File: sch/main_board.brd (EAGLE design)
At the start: 70 x 50 mm, 19 parts, among them IC1 MCP73831T-2ACI_OT, J1 MICRO_USB_B_HIROSE_ZX62-B-5PA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

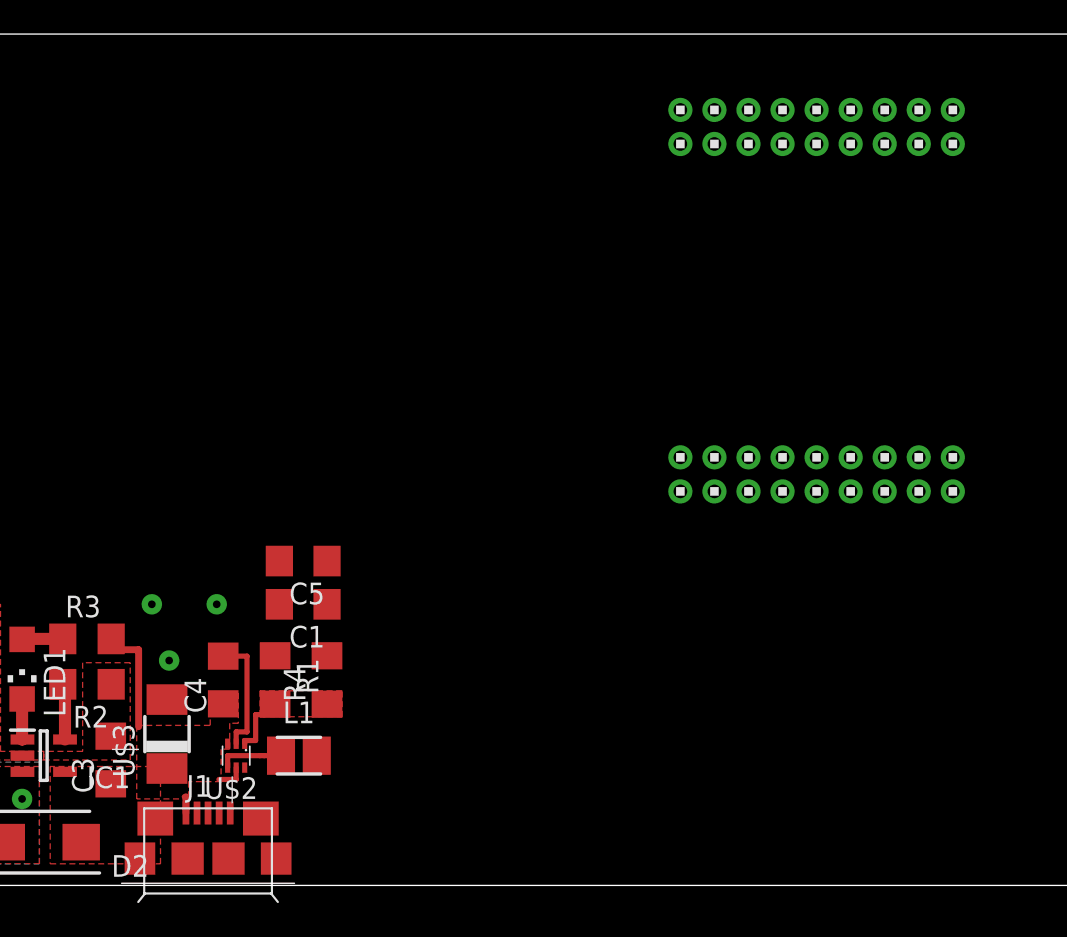
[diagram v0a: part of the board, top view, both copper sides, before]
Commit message: Add docs for STM32WB, Remove unused power supply elements.
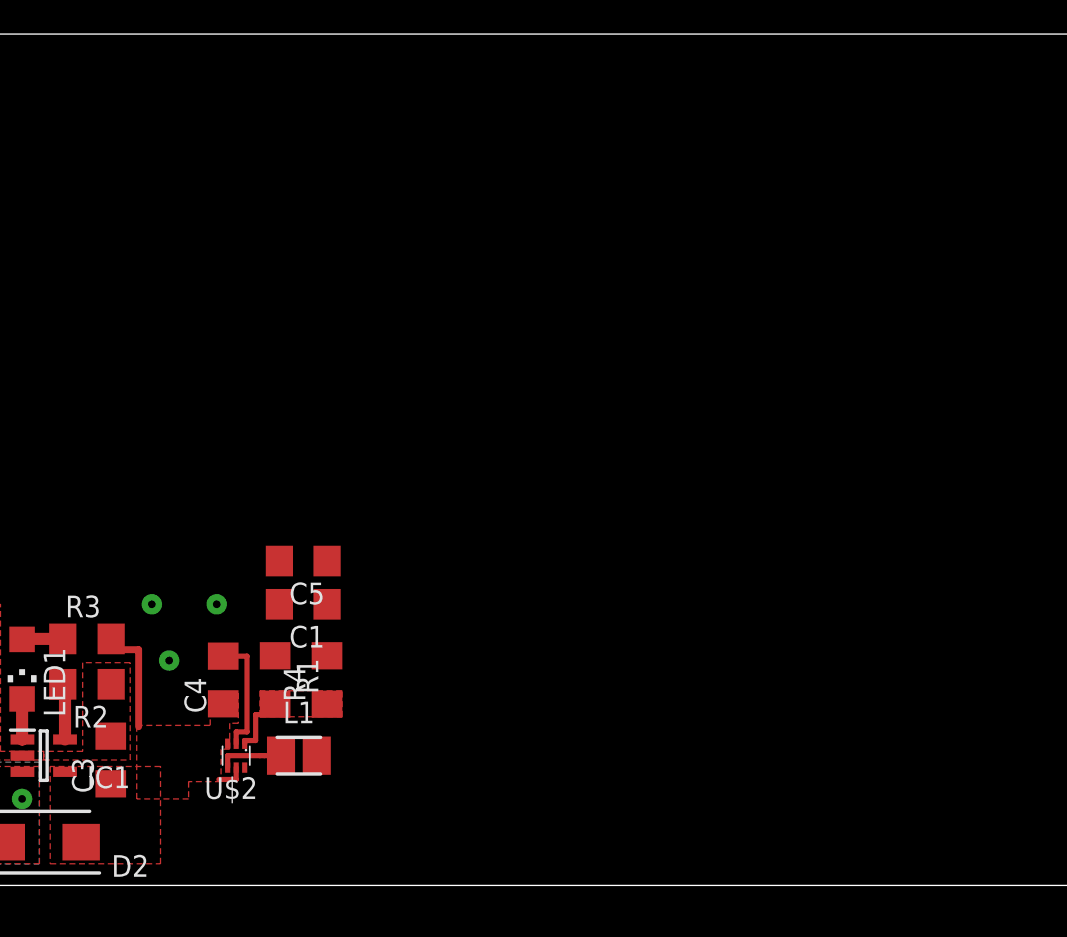
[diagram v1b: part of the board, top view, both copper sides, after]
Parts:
- removed J1: MICRO_USB_B_HIROSE_ZX62-B-5PA(11), connector:USB_MICRO_B-HIROSE-ZX62-B-5PA(11)
- removed U$3: SMAJ5.0A, SamacSys_Parts:DO-214AC
- removed U$6, U$7: 2X9, headers(2mm):2X9
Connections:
- removed net ID: J1.4
- removed net P0.00: U$6.14
- removed net P0.01: U$6.15
- removed net P0.02: U$6.16
- removed net P0.03: U$6.17
- removed net P0.04: U$6.18
- removed net P0.05: U$7.17
- removed net P0.06: U$7.18
- removed net P0.07: U$7.15
- removed net P0.08: U$7.16
- removed net P0.09: U$7.13
- removed net P0.10: U$7.14
- removed net P0.11: U$7.11
- removed net P0.12: U$7.12
- removed net P0.13: U$7.9
- removed net P0.14: U$7.10
- removed net P0.15: U$7.7
- removed net P0.16: U$7.8
- removed net P0.17: U$7.3
- removed net P0.18: U$7.1
- removed net P0.19: U$7.4
- removed net P0.20: U$7.2
- removed net P0.21: U$6.2
- removed net P0.22: U$6.3
- removed net P0.23: U$6.4
- removed net P0.24: U$6.5
- removed net P0.25: U$6.6
- removed net P0.28: U$6.9
- removed net P0.29: U$6.10
- removed net P0.30: U$6.13
- removed net SWDCLK: U$7.6
- removed net SWDIO: U$7.5
- removed net USB_D+: J1.3
- removed net USB_D-: J1.2
- net GND: no longer J1.5, U$3.A, U$6.1, U$6.12
- net VCC: no longer U$6.11
- net V_USB: no longer J1.1, U$3.C
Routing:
- net V_USB: track 9.53 -> 8.48 mm
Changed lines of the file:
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@@
 <?xml version="1.0" encoding="utf-8"?>
 <!DOCTYPE eagle SYSTEM "eagle.dtd">
-<eagle version="9.4.0">
+<eagle version="9.4.2">
 <drawing>
 <settings>
@@
 <dimension x1="0" y1="50" x2="0" y2="0" x3="-20" y3="25" textsize="1.778" layer="47" dtype="horizontal"/>
 <dimension x1="0" y1="0" x2="70" y2="0" x3="35" y3="-20" textsize="1.778" layer="47" dtype="horizontal"/>
-<wire x1="60.74" y1="21.969" x2="60.74" y2="46.985" width="0.1524" layer="51"/>
-<wire x1="60.74" y1="46.985" x2="28.74" y2="46.985" width="0.1524" layer="51"/>
-<wire x1="60.74" y1="21.969" x2="28.74" y2="21.969" width="0.1524" layer="51"/>
-<wire x1="28.74" y1="21.969" x2="28.74" y2="46.985" width="0.1524" layer="51"/>
 <dimension x1="59.74" y1="23.13" x2="59.73" y2="45.58" x3="63.50285" y3="34.356678125" textsize="1.778" layer="47"/>
 </plain>
@@
 <attribute name="VALUE" x="18.923" y="10.16" size="1.27" layer="27" rot="R180"/>
 </element>
-<element name="U$3" library="SamacSys_Parts" package="DO-214AC" value="SMAJ5.0A" x="13.589" y="8.89" smashed="yes" rot="R90">
-<attribute name="NAME" x="11.684" y="6.35" size="1.27" layer="25" rot="R90"/>
-<attribute name="VALUE" x="16.764" y="6.35" size="1.27" layer="27" rot="R90"/>
-</element>
 <element name="D2" library="SamacSys_Parts" package="DIOM5436X244N" value="VS-10BQ015-M3_5BT" x="6.35" y="2.54" smashed="yes" rot="R180">
 <attribute name="DESCRIPTION" value="VS-10BQ015-M3/5BT Vishay SMT Schottky Diode, 15V 1A, 2-Pin DO-214AA (SMB)" x="6.35" y="2.54" size="1.778" layer="27" rot="R180" display="off"/>
@@
 <attribute name="VALUE" x="7.62" y="11.938" size="1.27" layer="27"/>
 </element>
-<element name="J1" library="connector" package="USB_MICRO_B-HIROSE-ZX62-B-5PA(11)" value="MICRO_USB_B_HIROSE_ZX62-B-5PA(11)" x="16.002" y="0.127" smashed="yes">
-<attribute name="DIGIKEY" value="H11634CT-ND" x="16.002" y="0.127" size="1.778" layer="27" display="off"/>
-<attribute name="MOUSER" value="798-ZX62-B-5PA11" x="16.002" y="0.127" size="1.778" layer="27" display="off"/>
-<attribute name="NAME" x="14.732" y="5.207" size="1.27" layer="25" font="vector" ratio="12"/>
-<attribute name="NEWARK" value="86P8793" x="16.002" y="0.127" size="1.778" layer="27" display="off"/>
-<attribute name="VALUE" x="14.732" y="-6.223" size="1.27" layer="27" font="vector" ratio="12"/>
-</element>
 <element name="C2" library="resistor" library_urn="urn:adsk.eagle:library:348" package="C1206" package3d_urn="urn:adsk.eagle:package:23618/2" value="4.7u" x="2.667" y="7.366" smashed="yes" rot="R90">
 <attribute name="NAME" x="3.318" y="2.241" size="1.27" layer="25" rot="R90"/>
@@
 <attribute name="VALUE" x="22.86" y="21.59" size="1.27" layer="27" rot="R180"/>
 </element>
-<element name="U$6" library="headers(2mm)" package="2X9" value="2X9" x="51.74" y="24.14" smashed="yes"/>
-<element name="U$7" library="headers(2mm)" package="2X9" value="2X9" x="51.74" y="44.544" smashed="yes"/>
 </elements>
 <signals>
 <signal name="GND">
 <contactref element="U$1" pad="M"/>
-<contactref element="J1" pad="5"/>
-<contactref element="U$3" pad="A"/>
 <contactref element="C2" pad="2"/>
 <contactref element="R2" pad="1"/>
@@
 <wire x1="18.288" y1="9.017" x2="18.288" y2="13.465" width="0.3048" layer="1"/>
 <wire x1="18.288" y1="13.465" x2="16.891" y2="13.465" width="0.3048" layer="1"/>
-<contactref element="U$6" pad="1"/>
-<contactref element="U$6" pad="12"/>
-<wire x1="43.74" y1="23.14" x2="53.74" y2="25.14" width="0" layer="19" extent="1-1"/>
-<wire x1="20.19" y1="19.05" x2="43.74" y2="23.14" width="0" layer="19" extent="1-1"/>
 <wire x1="20.19" y1="16.51" x2="20.19" y2="19.05" width="0" layer="19" extent="1-1"/>
 <wire x1="19.939" y1="13.487" x2="20.19" y2="16.51" width="0" layer="19" extent="1-1"/>
 <wire x1="18.288" y1="13.465" x2="19.939" y2="13.487" width="0" layer="19" extent="1-1"/>
-<wire x1="17.302" y1="4.252" x2="17.653" y2="8.32" width="0" layer="19" extent="1-1"/>
-<wire x1="13.589" y1="10.915" x2="16.891" y2="13.465" width="0" layer="19" extent="1-1"/>
-<wire x1="10.312" y1="11.811" x2="13.589" y2="10.915" width="0" layer="19" extent="1-1"/>
+<wire x1="10.312" y1="11.811" x2="16.891" y2="13.465" width="0" layer="19" extent="1-1"/>
 <wire x1="2.667" y1="8.866" x2="2.667" y2="8.766" width="0" layer="19" extent="1-16"/>
 </signal>
@@
 </signal>
 <signal name="V_USB" class="2">
-<contactref element="J1" pad="1"/>
-<contactref element="U$3" pad="C"/>
 <contactref element="R3" pad="2"/>
 <contactref element="D2" pad="1"/>
@@
 <contactref element="C4" pad="1"/>
 <contactref element="U$2" pad="5"/>
-<wire x1="14.702" y1="4.252" x2="14.702" y2="5.207" width="0.4064" layer="1"/>
-<wire x1="14.702" y1="5.207" x2="14.605" y2="5.207" width="0.3048" layer="1"/>
 <wire x1="17.653" y1="6.92" x2="17.653" y2="6.223" width="0.3048" layer="1"/>
 <wire x1="17.653" y1="6.223" x2="16.637" y2="6.223" width="0.3048" layer="1"/>
-</signal>
-<signal name="USB_D-">
-<contactref element="J1" pad="2"/>
-</signal>
-<signal name="USB_D+">
-<contactref element="J1" pad="3"/>
-</signal>
-<signal name="ID">
-<contactref element="J1" pad="4"/>
 </signal>
 <signal name="N$3" class="1">
@@
 <contactref element="L1" pad="2"/>
 <contactref element="R4" pad="2"/>
-<contactref element="U$6" pad="11"/>
-<wire x1="22.99" y1="19.05" x2="53.74" y2="23.14" width="0" layer="19" extent="1-1"/>
 <wire x1="22.99" y1="16.51" x2="22.99" y2="19.05" width="0" layer="19" extent="1-1"/>
 <wire x1="22.987" y1="13.487" x2="22.99" y2="16.51" width="0" layer="19" extent="1-1"/>
 <wire x1="22.386" y1="7.62" x2="22.987" y2="13.487" width="0" layer="19" extent="1-1"/>
 </signal>
-<signal name="P0.20">
-<contactref element="U$7" pad="2"/>
-</signal>
-<signal name="P0.18">
-<contactref element="U$7" pad="1"/>
-</signal>
-<signal name="P0.06">
-<contactref element="U$7" pad="18"/>
-</signal>
-<signal name="P0.05">
-<contactref element="U$7" pad="17"/>
-</signal>
-<signal name="P0.21">
-<contactref element="U$6" pad="2"/>
-</signal>
-<signal name="P0.04">
-<contactref element="U$6" pad="18"/>
-</signal>
-<signal name="P0.23">
-<contactref element="U$6" pad="4"/>
-</signal>
-<signal name="P0.25">
-<contactref element="U$6" pad="6"/>
-</signal>
-<signal name="P0.29">
-<contactref element="U$6" pad="10"/>
-</signal>
-<signal name="P0.00">
-<contactref element="U$6" pad="14"/>
-</signal>
-<signal name="P0.02">
-<contactref element="U$6" pad="16"/>
-</signal>
-<signal name="P0.17">
-<contactref element="U$7" pad="3"/>
-</signal>
-<signal name="SWDIO">
-<contactref element="U$7" pad="5"/>
-</signal>
-<signal name="P0.15">
-<contactref element="U$7" pad="7"/>
-</signal>
-<signal name="P0.13">
-<contactref element="U$7" pad="9"/>
-</signal>
-<signal name="P0.11">
-<contactref element="U$7" pad="11"/>
-</signal>
-<signal name="P0.09">
-<contactref element="U$7" pad="13"/>
-</signal>
-<signal name="P0.07">
-<contactref element="U$7" pad="15"/>
-</signal>
-<signal name="P0.19">
-<contactref element="U$7" pad="4"/>
-</signal>
-<signal name="SWDCLK">
-<contactref element="U$7" pad="6"/>
-</signal>
-<signal name="P0.16">
-<contactref element="U$7" pad="8"/>
-</signal>
-<signal name="P0.14">
-<contactref element="U$7" pad="10"/>
-</signal>
-<signal name="P0.12">
-<contactref element="U$7" pad="12"/>
-</signal>
-<signal name="P0.10">
-<contactref element="U$7" pad="14"/>
-</signal>
-<signal name="P0.08">
-<contactref element="U$7" pad="16"/>
-</signal>
-<signal name="P0.03">
-<contactref element="U$6" pad="17"/>
-</signal>
-<signal name="P0.22">
-<contactref element="U$6" pad="3"/>
-</signal>
-<signal name="P0.24">
-<contactref element="U$6" pad="5"/>
-</signal>
-<signal name="P0.28">
-<contactref element="U$6" pad="9"/>
-</signal>
-<signal name="P0.30">
-<contactref element="U$6" pad="13"/>
-</signal>
-<signal name="P0.01">
-<contactref element="U$6" pad="15"/>
-</signal>
 </signals>

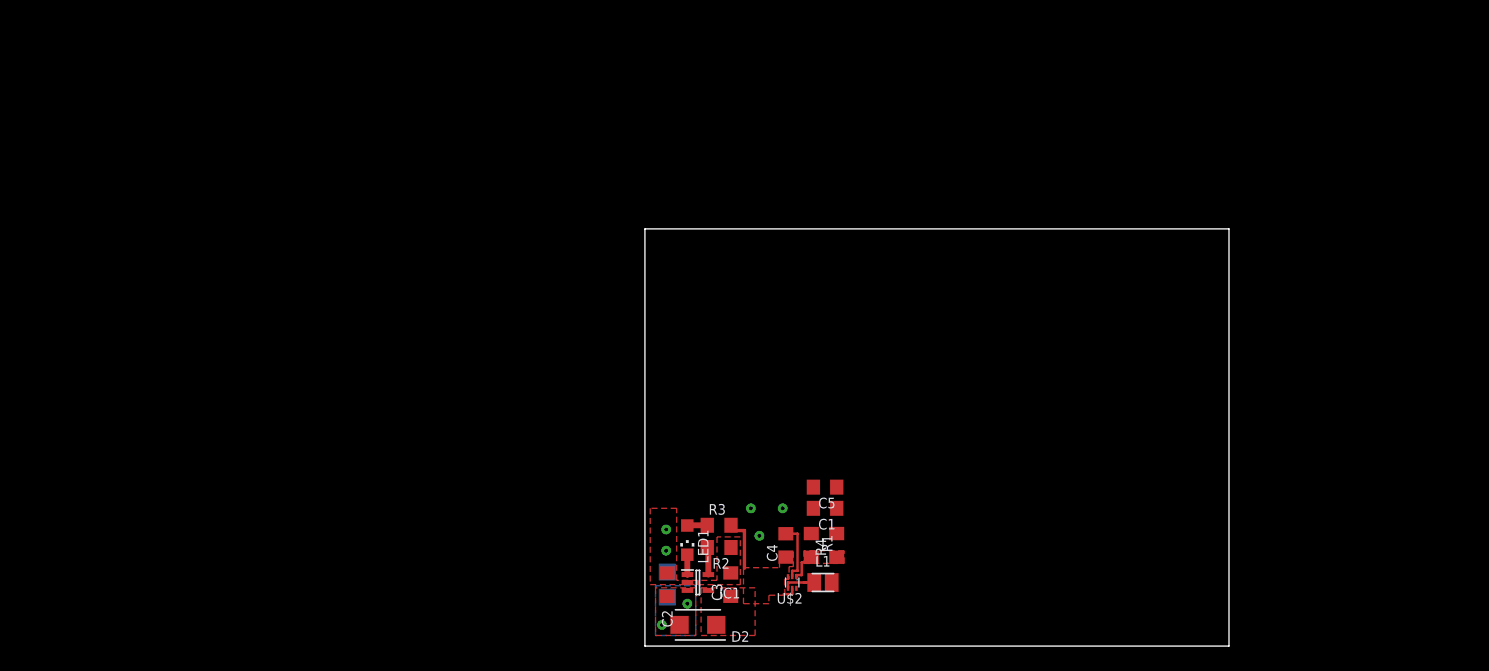
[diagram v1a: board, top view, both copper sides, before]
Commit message: Add library for STM32WB prototype board.
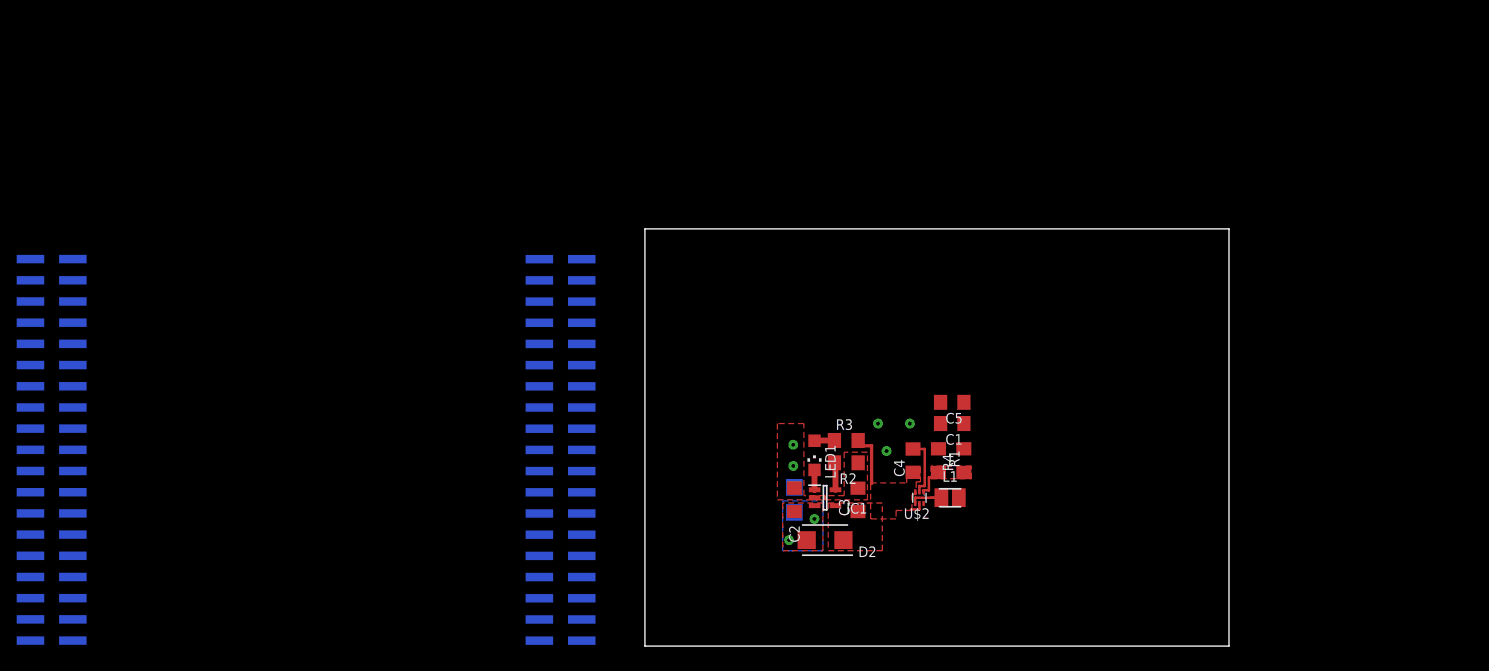
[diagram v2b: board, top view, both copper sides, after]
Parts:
- added U$3: STM32_NUCLEO-68_WB, STM32WB:STM32_NUCLEO-68_FOOTPRINT
- moved C4 18.3 mm to (32.1, 22.2)
- moved L1 18.3 mm to (36.6, 17.8)
- moved R1 18.3 mm to (35.2, 22.2)
- moved U$2 18.3 mm to (32.9, 17.8)
- moved C1 18.3 mm to (36.8, 26.7)
- moved C2 18.3 mm to (17.9, 17.5)
- moved C3 18.3 mm to (25.5, 17.5)
- moved C5 18.3 mm to (36.8, 29.2)
- moved D2 18.3 mm to (21.6, 12.7)
- moved IC1 18.3 mm to (21.6, 17.8)
- moved LED1 18.3 mm to (20.3, 22.9)
- moved R2 18.3 mm to (24.1, 22.0)
- moved R3 18.3 mm to (24.1, 24.6)
- moved R4 18.3 mm to (38.2, 22.2)
- moved U$1 18.3 mm to (17.9, 17.5)
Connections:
- removed net V_USB: C3.1, C4.1, D2.1, IC1.4, R3.2, U$2.3, U$2.5
- new net 5V0: C3.1, C4.1, D2.1, IC1.4, R3.2, U$2.3, U$2.5, U$3.18
- net GND: now also U$3.19, U$3.20, U$3.47, U$3.58, U$3.70, U$3.8
- net VCC: now also U$3.5
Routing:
- net 5V0: track 0.00 -> 8.48 mm
- net V_USB: track 8.48 -> 0.00 mm
- added copper zone on layer 1, net 5V0
- removed copper zone on layer 1, net V_USB

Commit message: Add STM32WB board part, add sensor connector part
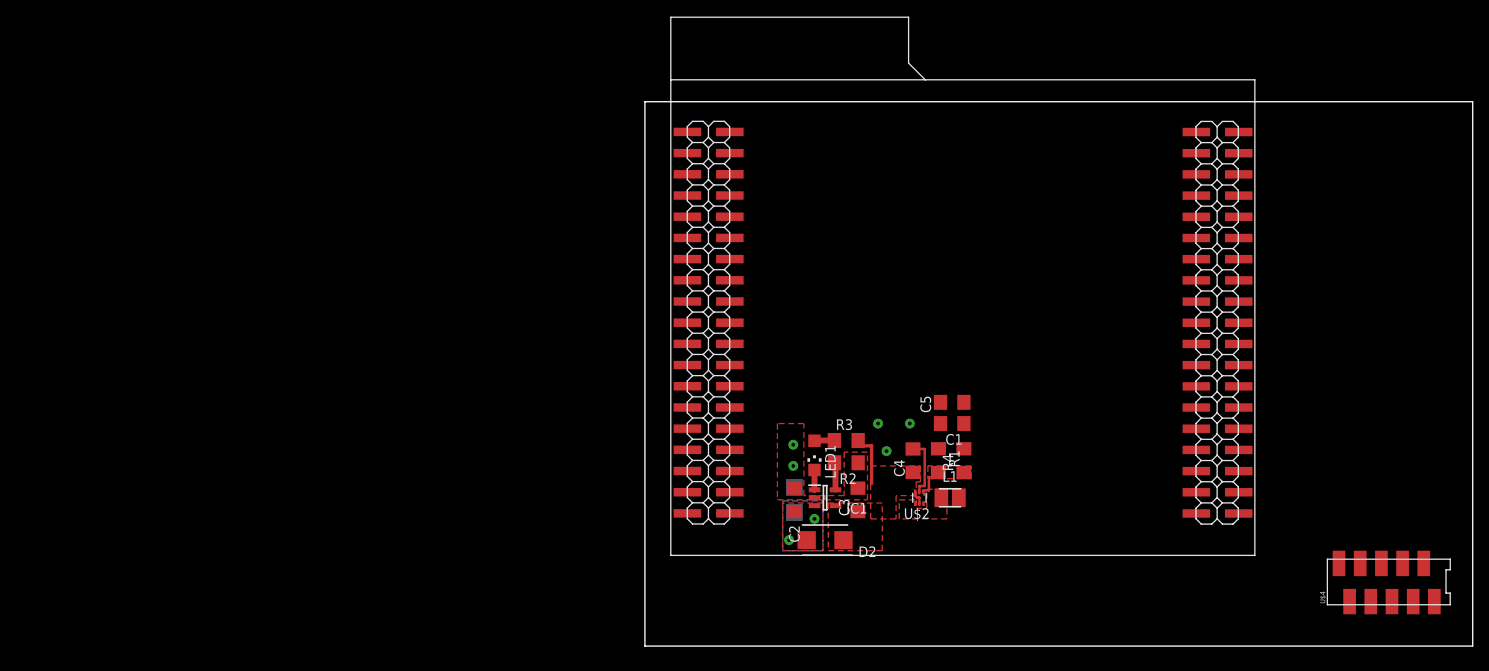
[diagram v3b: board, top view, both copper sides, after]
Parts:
- added U$4: (no value), SamacSys_Parts:1-2178712-0
- moved U$3 80.2 mm to (38.1, 39.4)
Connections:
- new net MPU_INT: U$3.34, U$4.P$5
- new net SPI_CS_0: U$3.73
- new net SPI_CS_1: U$3.75, U$4.P$6
- new net SPI_CS_2: U$3.55, U$4.P$7
- new net SPI_CS_3: U$3.49, U$4.P$8
- new net SPI_MISO: U$3.51, U$4.P$9
- new net SPI_MOSI: U$3.53, U$4.P$4
- new net SPI_SCK: U$3.32, U$4.P$3
- net GND: now also U$4.P$1, U$4.P$10
- net VCC: now also U$4.P$2
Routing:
- net N$6: track 3.83 -> 0.00 mm
- added copper zone on layer 1, net N$6
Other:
- board size 70 x 50 mm -> 99.2 x 65.2 mm
